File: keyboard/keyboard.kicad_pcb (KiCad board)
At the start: 2 copper layers, 119 parts, among them J1 AudioJack4, SW1 SW_Push_45deg, SW10 SW_Push_45deg, SW11 SW_Push_45deg, SW12 SW_Push_45deg, SW13 SW_Push_45deg, SW14 SW_Push_45deg, SW15 SW_Push_45deg, SW16 SW_Push_45deg, SW17 SW_Push_45deg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

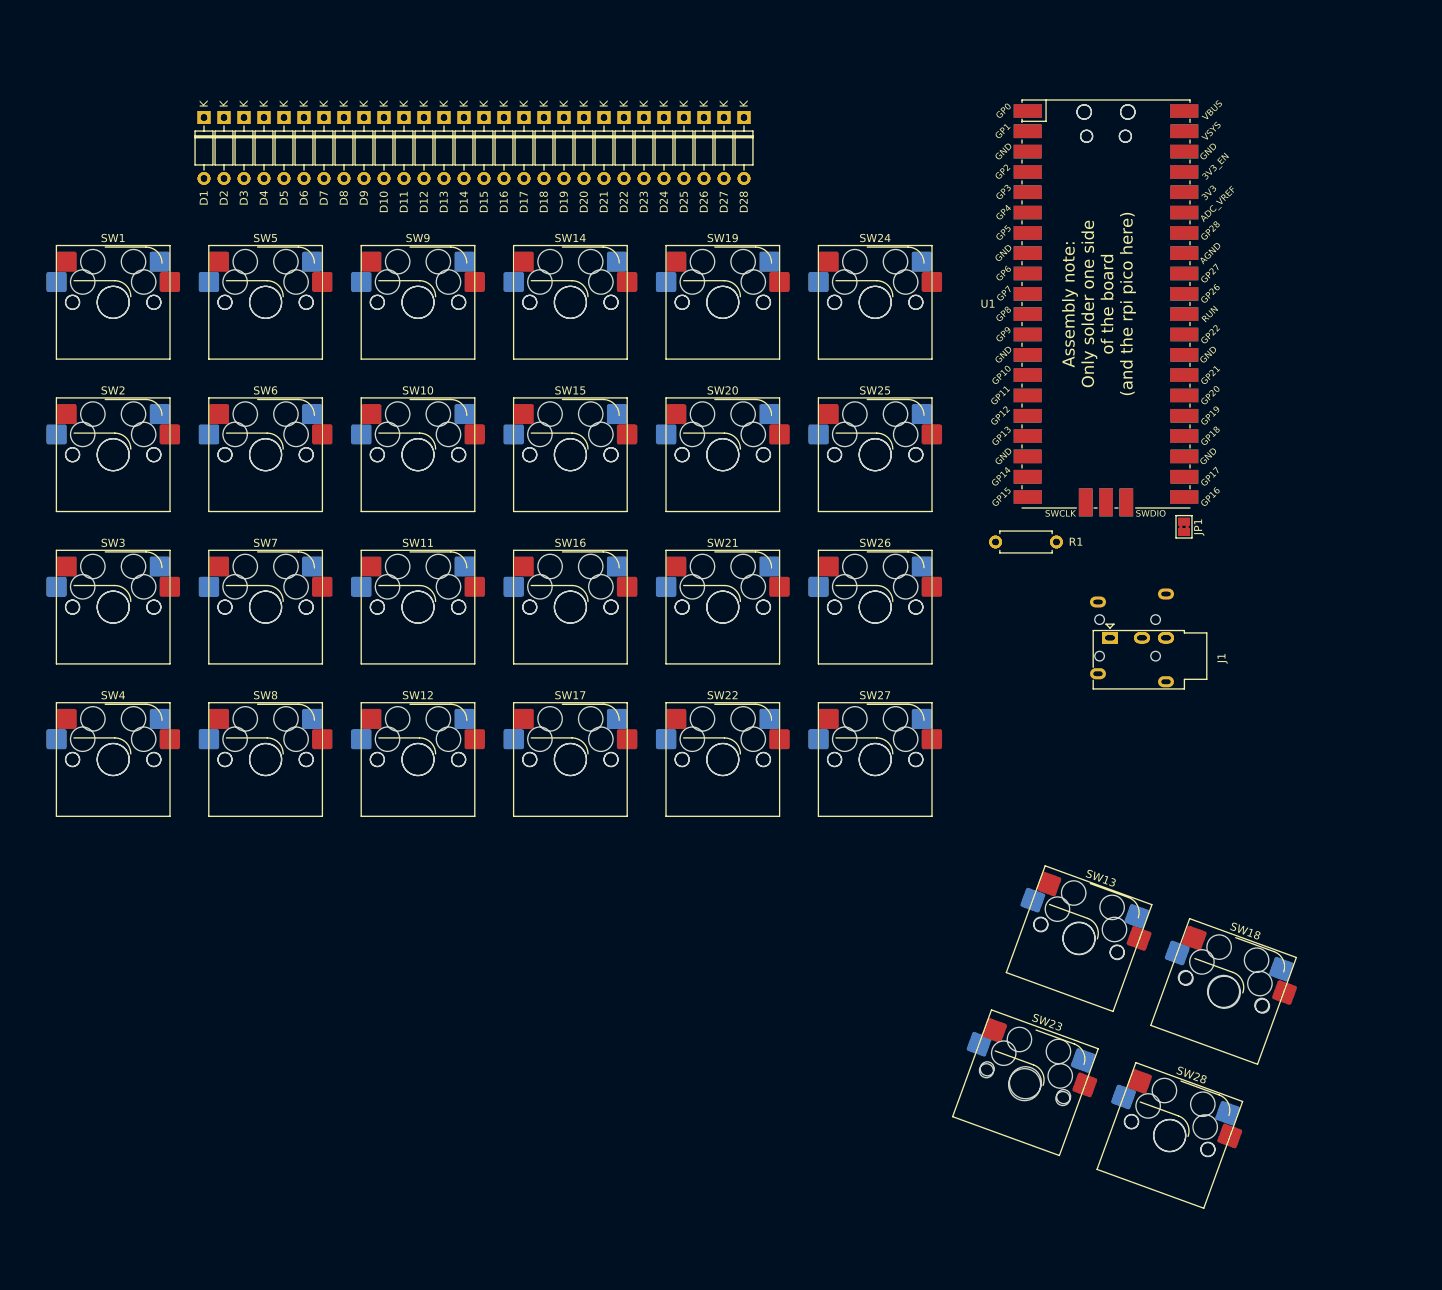
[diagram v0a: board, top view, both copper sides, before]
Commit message: add peekabu logo
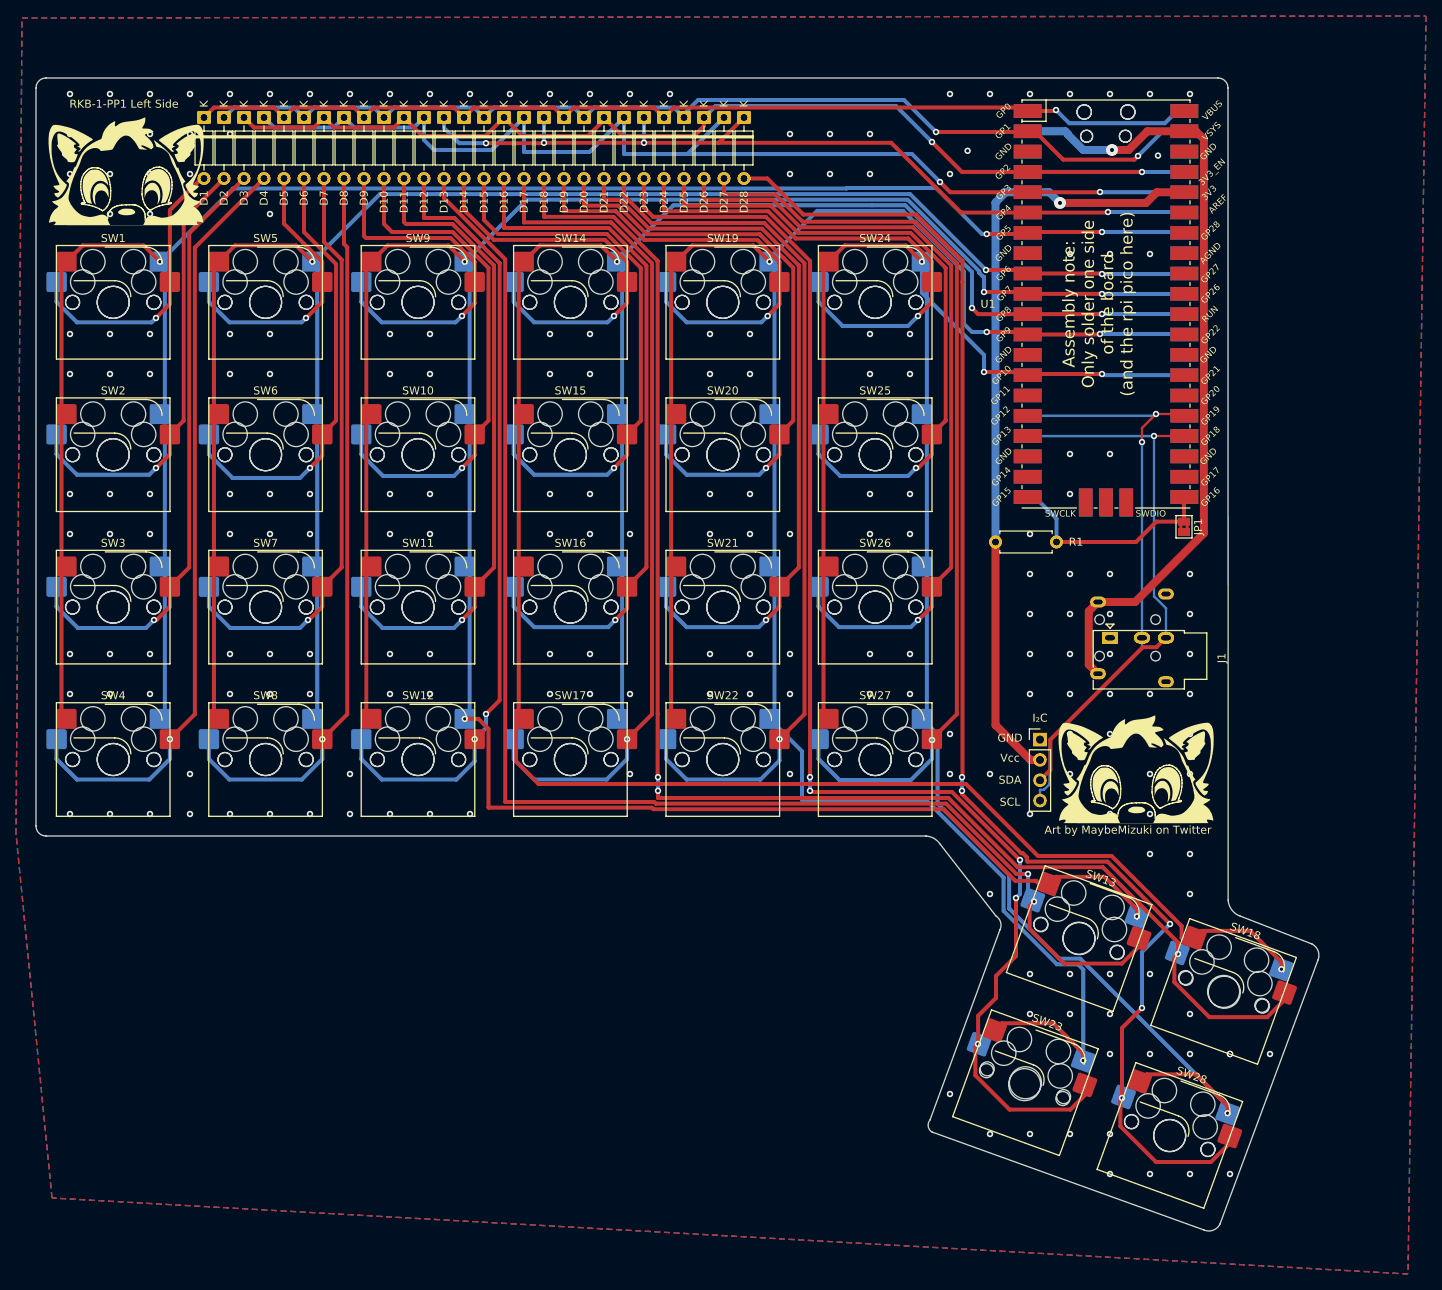
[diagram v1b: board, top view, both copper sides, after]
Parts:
- added G***: LOGO, Symbols:lotte-peekabu, F.Cu at (153.2, 124.2)
- added G***: LOGO, Symbols:lotte-peekabu, F.Cu at (27.0, 49.5)
- added G***: LOGO, Symbols:lotte-peekabu, B.Cu at (153.2, 124.2)
- added G***: LOGO, Symbols:lotte-peekabu, B.Cu at (27.0, 49.5)
- added REF**: PinHeader_1x04_P2.54mm_Vertical, Connector_PinHeader_2.54mm:PinHeader_1x04_P2.54mm_Vertical, F.Cu at (141.2, 120.7)
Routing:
- net /COL2: track 0.00 -> 330.4 mm, vias 0 -> 5
- net /COL3: track 0.00 -> 326.2 mm, vias 0 -> 4
- net /COL4: track 0.00 -> 278.3 mm, vias 0 -> 4
- net /COL0: track 0.00 -> 264.2 mm, vias 0 -> 3
- net /COL5: track 0.00 -> 252.9 mm, vias 0 -> 4
- net /COL1: track 0.00 -> 246.5 mm, vias 0 -> 3
- net Net-(D18-Pad2): track 0.00 -> 183.5 mm, vias 0 -> 3
- net Net-(D28-Pad2): track 0.00 -> 176.7 mm, vias 0 -> 5
- net Net-(D13-Pad2): track 0.00 -> 174.7 mm, vias 0 -> 2
- net Net-(D23-Pad2): track 0.00 -> 169.9 mm, vias 0 -> 5
- net /ROW3: track 0.00 -> 140.3 mm, vias 0 -> 2
- net /ROW1: track 0.00 -> 130.1 mm, vias 0 -> 2
- net /ROW2: track 0.00 -> 129.3 mm, vias 0 -> 2
- net /ROW0: track 0.00 -> 128.9 mm, vias 0 -> 1
- net Net-(D27-Pad2): track 0.00 -> 116.7 mm, vias 0 -> 1
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- added copper zone on B.Cu, net GND
- added copper zone on F.Cu, net GND
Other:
- board outline added: 160.4 x 144.1 mm
- board text added: "Art by MaybeMizuki on Twitter"
- board text added: "GND"
- board text added: "I₂C"
- board text added: "RKB-1-PP1 Left Side"
- board text added: "RKB-1-PP1 Right Side"
- board text added: "SCL"
- board text added: "SDA"
- board text added: "Vcc"
